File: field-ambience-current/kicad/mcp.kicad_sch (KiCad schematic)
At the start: 45 parts, among them SW1 Cell 1 (2u Choc V2 Hot-Swap), SW10 Modifier CLEAR (12x12x7.3 SMD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, SW2 Cell 2 (2u Choc V2 Hot-Swap), SW3 Cell 3 (2u Choc V2 Hot-Swap), SW4 Cell 4 (2u Choc V2 Hot-Swap), SW5 Cell 5 (2u Choc V2 Hot-Swap), SW6 Modifier SHIFT (12x12x7.3 SMD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, SW7 Modifier HOLD (12x12x7.3 SMD-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, SW8 Modifier DRONE (12x12x7.3 SMD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, SW9 Modifier GENERATE (12x12x7.3 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, U2 MCP23017-E/SS (I/O-Expander), U6 PCA9685PW (16-Ch I²C PWM LED-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

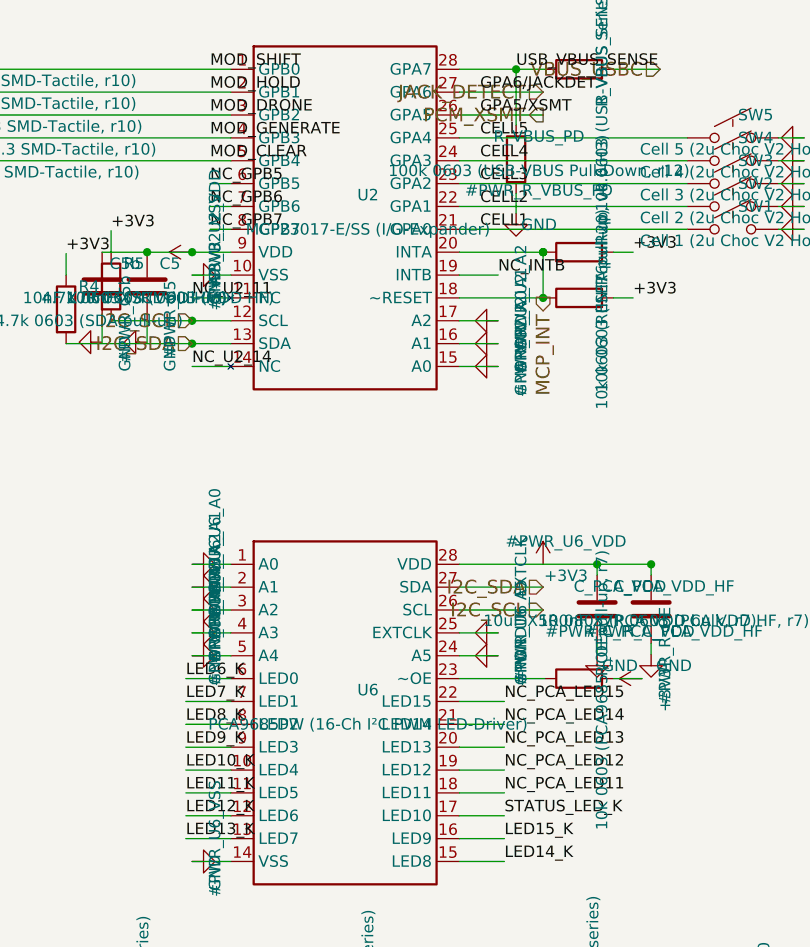
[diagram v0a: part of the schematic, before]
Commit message: pcb(r18.5): Schematic-Migration Phase 3 — STM32H743 + LCD im Generator, Repo-Audit-Fixes
KERN: generate_kicad_project.py erzeugt jetzt die H7-Architektur.

NEU stm32h743.kicad_sch (ersetzt pico.kicad_sch -> kicad/legacy_pico2/):
- 100-Pin-Symbol 1:1 aus offizieller KiCad-Lib (MCU_ST_STM32H7),
  doppelt verifiziert gegen SPEC v0.7 §5 / DS12110 Rev 5 Table 8 —
  alle 52 belegten Zuordnungen identisch (zwei unabhängige Quellen)
- alle SPEC-§5-Netze verdrahtet, 48 Reserve-GPIOs no_connect
- Support: HSE Y1 ABLS-8.000MHZ-B4-T (C596838) + 2x22pF, VCAP 2x2.2uF
  (DS12110 Tab.24), 5x(4.7uF+100nF) VDD-Bank, VDDA-Ferrit C84094 +
  1uF+100nF, BOOT0-PD 10k, NRST-PU 10k+100nF, SWD-J4 (PA13/PA14/GND),
  BAT-Teiler 100k/100k+10nF an PA3, Status-LED PD8, USB-FS PA11/PA12
  (USBLC6-ESD bleibt davor), MIDI_TX-Netz (PD5)

NEU lcd.kicad_sch (ersetzt oled.kicad_sch -> legacy): 8-Pin-ST7789
per SPEC §6 + C6b/C6c + Backlight: PCA9685-Kanal-12 -> LCD_BLK_PWM ->
2N7002 Low-Side + 100k-PD. Netze OLED_* -> LCD_*.

power_tree: U5 AP7361A-33 LDO (+5V->+3V3) + Cin 1uF/Cout 2.2uF +
EN->IN. Pico-SMPS entfällt. PICO_USB_* -> USB_DM/USB_DP.

mcp: GPB5 = VOL_SW (SPEC §5.4 — lag bis r17 entgegen der SPEC am
Pico-GPIO), PCA-Kanal 12 = LCD_BLK_PWM. Root-Brücken umgebaut,
kicad_pro-Sheetliste: Battery ergänzt (fehlte).

AUDIT-FINDINGS (verifiziert, nicht aus dem Alt-Audit übernommen):
- F-6 NEU 🔴: SPEC-§4-U5-LCSC C156144 ist ein 910R-WIDERSTAND
  (LCSC-Web verifiziert) — hätte bei JLC einen R als LDO bestückt.
  SPEC korrigiert (Kandidat C150719), Symbol trägt TBD-VERIFY.
- B-LDO 🔴: AP7361A-SOT-89-5-Pinout-Annahme (1=ADJ/NC,2=OUT,3=IN,
  4=GND,5=EN aus AP7361-DS33626-Lesart; A-Datasheet war HTTP 403) —
  als PIN_VERIFY am Symbol + PCB_LAYOUT_STATUS dokumentiert.
- B-SW12 🔴: SW6-10 (HX 12x12) auf ~6mm-TL3342-Pattern — als
  FP_MISMATCH-Property an allen 5 Symbolen markiert.
- F-2-Teilfix: Encoder-MPN -> EC11J1525402, Bourns-PEC11R-PDF nach
  datasheets/legacy/ (falsches Teil); ALPS-Drawing offen.
- F-1: T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
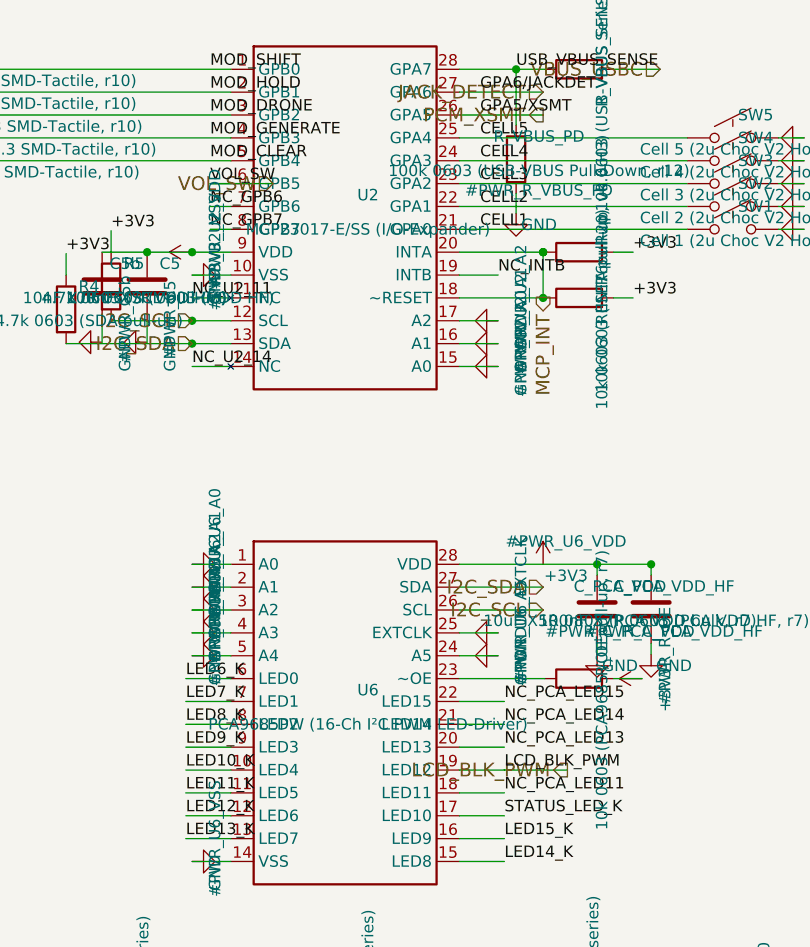
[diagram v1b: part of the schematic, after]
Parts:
- SW10, SW6, SW7, SW8, SW9: FP_MISMATCH (none) -> B-SW12: SW_SPST_TL3342 ist ein ~6mm-Land-Pattern, Teil ist 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
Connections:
- net NC_GPB5 renamed VOL_SW
- net NC_PCA_LED12 renamed LCD_BLK_PWM
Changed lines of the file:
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@@
       (property "LCSC" "C36498966" (at 87.46000000000001 98.57 0)
+        (effects (font (size 1.27 1.27)) hide))
+      (property "FP_MISMATCH" "B-SW12: SW_SPST_TL3342 ist ein ~6mm-Land-Pattern, Teil ist 12x12mm — vor Layout eigenen 12x12-SMD-FP anlegen + gegen HX-Datasheet (C36498966) pruefen" (at 87.46000000000001 99.83999999999999 0)
         (effects (font (size 1.27 1.27)) hide))
     (instances
@@
       (property "LCSC" "C36498966" (at 87.46000000000001 101.11 0)
         (effects (font (size 1.27 1.27)) hide))
+      (property "FP_MISMATCH" "B-SW12: SW_SPST_TL3342 ist ein ~6mm-Land-Pattern, Teil ist 12x12mm — vor Layout eigenen 12x12-SMD-FP anlegen + gegen HX-Datasheet (C36498966) pruefen" (at 87.46000000000001 102.38 0)
+        (effects (font (size 1.27 1.27)) hide))
     (instances
       (project "field_ambience"
@@
       (property "LCSC" "C36498966" (at 87.46000000000001 103.64999999999999 0)
         (effects (font (size 1.27 1.27)) hide))
+      (property "FP_MISMATCH" "B-SW12: SW_SPST_TL3342 ist ein ~6mm-Land-Pattern, Teil ist 12x12mm — vor Layout eigenen 12x12-SMD-FP anlegen + gegen HX-Datasheet (C36498966) pruefen" (at 87.46000000000001 104.91999999999999 0)
+        (effects (font (size 1.27 1.27)) hide))
     (instances
       (project "field_ambience"
@@
       (property "LCSC" "C36498966" (at 87.46000000000001 106.19 0)
         (effects (font (size 1.27 1.27)) hide))
+      (property "FP_MISMATCH" "B-SW12: SW_SPST_TL3342 ist ein ~6mm-Land-Pattern, Teil ist 12x12mm — vor Layout eigenen 12x12-SMD-FP anlegen + gegen HX-Datasheet (C36498966) pruefen" (at 87.46000000000001 107.46 0)
+        (effects (font (size 1.27 1.27)) hide))
     (instances
       (project "field_ambience"
@@
       (property "LCSC" "C36498966" (at 87.46000000000001 108.72999999999999 0)
         (effects (font (size 1.27 1.27)) hide))
+      (property "FP_MISMATCH" "B-SW12: SW_SPST_TL3342 ist ein ~6mm-Land-Pattern, Teil ist 12x12mm — vor Layout eigenen 12x12-SMD-FP anlegen + gegen HX-Datasheet (C36498966) pruefen" (at 87.46000000000001 109.99999999999999 0)
+        (effects (font (size 1.27 1.27)) hide))
     (instances
       (project "field_ambience"
@@
     (stroke (width 0) (type default))
 )
+  (wire (pts (xy 115 106.19) (xy 122 106.19))
+    (stroke (width 0) (type default))
+)
   (wire (pts (xy 117.3 108.72999999999999) (xy 115 108.72999999999999))
     (stroke (width 0) (type default))
@@
     (stroke (width 0) (type default))
 )
+  (wire (pts (xy 147.7 171.35000000000002) (xy 154.7 171.35000000000002))
+    (stroke (width 0) (type default))
+)
   (wire (pts (xy 142.7 168.81) (xy 147.7 168.81))
     (stroke (width 0) (type default))
@@
     (effects (font (size 1.27 1.27)) (justify left bottom))
 )
-  (label "NC_GPB5" (at 115 106.19 0) (fields_autoplaced)
+  (label "VOL_SW" (at 115 106.19 0) (fields_autoplaced)
     (effects (font (size 1.27 1.27)) (justify left bottom))
 )
@@
     (effects (font (size 1.27 1.27)) (justify left bottom))
 )
-  (label "NC_PCA_LED12" (at 147.7 171.35000000000002 0) (fields_autoplaced)
+  (label "LCD_BLK_PWM" (at 147.7 171.35000000000002 0) (fields_autoplaced)
     (effects (font (size 1.27 1.27)) (justify left bottom))
 )
@@
     (effects (font (size 1.524 1.524)) (justify right))
 )
+  (hierarchical_label "VOL_SW" (shape input) (at 122 106.19 180)
+    (effects (font (size 1.524 1.524)) (justify right))
+)
   (hierarchical_label "PCM_XSMT" (shape output) (at 152 98.57 180)
     (effects (font (size 1.524 1.524)) (justify right))
@@
     (effects (font (size 1.524 1.524)) (justify right))
 )
+  (hierarchical_label "LCD_BLK_PWM" (shape output) (at 154.7 171.35000000000002 180)
+    (effects (font (size 1.524 1.524)) (justify right))
+)

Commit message: pcb(r18.6): Engineering-Verifikation — AP7361C-Pinout-Fix, TPS61089-Quelle, Custom-FP, BOM-LCSC, ADR-MIDI
Reaktion auf User-Korrekturen aus öffentlichen Datasheets. Vier
🔴-Blocker geschlossen, einer auf eine Design-Entscheidung umklassifiziert.

=== AP7361A-Pinout war FALSCH — gefixt + AP7361C ===

r18.5-Annahme: 1=ADJ/NC, 2=OUT, 3=IN, 4=GND, 5=EN.
Korrekt (Diodes-DS via mouser.de/datasheet/3/175/1/AP7361.pdf,
User-verifiziert):
    1=EN, 2=GND, 3=ADJ/NC, 4=IN, 5=OUT

Hätte zu einem totem Board geführt (IN/OUT/EN vertauscht).

Zusätzlich:
- Symbol auf AP7361C umbenannt (Diodes markiert AP7361 als NRND ->
  use AP7361C; gleicher SOT-89-5-Pinout)
- AP7361C-33Y5-13 = LCSC C460397 (SOT-89-5) statt r18.5-Kandidat
  C150719 (= SOT-223, falsches Package; verworfen)
- Cin/Cout 4.7 µF X5R 0603 (DS-Empfehlung, statt 1µF/2.2µF)
- Symbol-Pinmap + power_tree-Verdrahtung umgebaut: EN-Pin liegt
  jetzt links oben (statt links unten), IN links unten, OUT
  rechts oben — neu gerechnete Stub-Wires + Junctions

=== TPS61089-Footprint + Datenblatt-Anchor ===

- Symbol-Pinmap (1=FSW … 11=SW) verifiziert gegen TI Rev C Tabelle 6-1
  (User-Quelle ti.com/lit/gpn/tps61089) — als PIN_SOURCE-Property
- Footprint-Name auf RNR0011A-Konvention 2.0x2.5mm VQFN-HR
- RNSR-PDF → datasheets/legacy/TPS61089RNSR_wrong_variant.pdf

=== Encoder C209762 (NRND, Prototype-OK) ===

- MPN EC11J1525402, LCSC C209762 (JLCPCB-verifiziert)
- Datasheet-Link auf JLCPCB-Detail-Seite (ALPS-Drawing nicht öffentlich)
- Status: NRND als Property — Prototype-OK, Serie braucht Ersatztyp
- FP_VERIFY-Hinweis (EC11J ist SMD, der KiCad-Standard-FP EC11E ist THT)

=== Custom-Footprint für HX 12x12 (SW6-10) ===

- libraries/field_ambience.pretty/SW_HX_12x12x7.3_SMD-4P.kicad_mod
  basierend auf LCSC-Daten von C36498966:
  - SMD-4P, 11.8x11.8mm Body, 7.3mm Höhe
  - 4 Pads je 2.5x1.5mm auf 7mm-Pitch (X+Y)
  - SPST: gegenüberliegende Pads verbunden (1↔1, 2↔2)
  - Silkscreen + Pin-1-Dot + Courtyard +0.25mm IPC-7351B
- fp-lib-table um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
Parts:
- SW10, SW6, SW7, SW8, SW9: footprint Button_Switch_SMD:SW_SPST_TL3342 -> field_ambience:SW_HX_12x12x7.3_SMD-4P; FP_MISMATCH B-SW12: SW_SPST_TL3342 ist ein ~6mm-Land-Pattern, Teil ist 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 -> (none); FP_NOTE (none) -> Custom-Footprint libraries/field_ambience.pretty/SW_HX_12x1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; Manufacturer (none) -> hanxia; Package (none) -> SMD-4P 11.8x11.8mm, vertical tactile, 7.3mm height, SPST 25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
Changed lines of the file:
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@@
       (property "Value" "Modifier SHIFT (12x12x7.3 SMD-Tactile, r10)" (at 87.46000000000001 94.75999999999999 0)
         (effects (font (size 1.27 1.27))))
-      (property "Footprint" "Button_Switch_SMD:SW_SPST_TL3342" (at 84.92 93.49 0)
+      (property "Footprint" "field_ambience:SW_HX_12x12x7.3_SMD-4P" (at 84.92 93.49 0)
         (effects (font (size 1.27 1.27)) hide))
-      (property "Datasheet" "~" (at 84.92 93.49 0)
+      (property "Datasheet" "https://www.lcsc.com/product-detail/C36498966.html" (at 84.92 93.49 0)
         (effects (font (size 1.27 1.27)) hide))
       (property "MPN" "HX 12x12x7.3TPFT-B" (at 87.46000000000001 97.3 0)
         (effects (font (size 1.27 1.27)) hide))
-      (property "LCSC" "C36498966" (at 87.46000000000001 98.57 0)
+      (property "Manufacturer" "hanxia" (at 87.46000000000001 98.57 0)
         (effects (font (size 1.27 1.27)) hide))
-      (property "FP_MISMATCH" "B-SW12: SW_SPST_TL3342 ist ein ~6mm-Land-Pattern, Teil ist 12x12mm — vor Layout eigenen 12x12-SMD-FP anlegen + gegen HX-Datasheet (C36498966) pruefen" (at 87.46000000000001 99.83999999999999 0)
+      (property "LCSC" "C36498966" (at 87.46000000000001 99.83999999999999 0)
+        (effects (font (size 1.27 1.27)) hide))
+      (property "Package" "SMD-4P 11.8x11.8mm, vertical tactile, 7.3mm height, SPST 250gf, 100k cycles, 12V/50mA" (at 87.46000000000001 101.11 0)
+        (effects (font (size 1.27 1.27)) hide))
+      (property "FP_NOTE" "Custom-Footprint libraries/field_ambience.pretty/SW_HX_12x12x7.3_SMD-4P.kicad_mod (User-Daten + LCSC C36498966). 4 Pads je 2.5x1.5mm auf 7mm-Pitch (X+Y); SPST: gegenüberliegende Pads sind elektrisch verbunden (1↔1, 2↔2)." (at 87.46000000000001 102.38 0)
         (effects (font (size 1.27 1.27)) hide))
     (instances
@@
       (property "Value" "Modifier HOLD (12x12x7.3 SMD-Tactile, r10)" (at 87.46000000000001 97.3 0)
         (effects (font (size 1.27 1.27))))
-      (property "Footprint" "Button_Switch_SMD:SW_SPST_TL3342" (at 84.92 96.03 0)
+      (property "Footprint" "field_ambience:SW_HX_12x12x7.3_SMD-4P" (at 84.92 96.03 0)
         (effects (font (size 1.27 1.27)) hide))
-      (property "Datasheet" "~" (at 84.92 96.03 0)
+      (property "Datasheet" "https://www.lcsc.com/product-detail/C36498966.html" (at 84.92 96.03 0)
         (effects (font (size 1.27 1.27)) hide))
       (property "MPN" "HX 12x12x7.3TPFT-B" (at 87.46000000000001 99.84 0)
         (effects (font (size 1.27 1.27)) hide))
-      (property "LCSC" "C36498966" (at 87.46000000000001 101.11 0)
+      (property "Manufacturer" "hanxia" (at 87.46000000000001 101.11 0)
         (effects (font (size 1.27 1.27)) hide))
-      (property "FP_MISMATCH" "B-SW12: SW_SPST_TL3342 ist ein ~6mm-Land-Pattern, Teil ist 12x12mm — vor Layout eigenen 12x12-SMD-FP anlegen + gegen HX-Datasheet (C36498966) pruefen" (at 87.46000000000001 102.38 0)
+      (property "LCSC" "C36498966" (at 87.46000000000001 102.38 0)
+        (effects (font (size 1.27 1.27)) hide))
+      (property "Package" "SMD-4P 11.8x11.8mm, vertical tactile, 7.3mm height, SPST 250gf, 100k cycles, 12V/50mA" (at 87.46000000000001 103.65 0)
+        (effects (font (size 1.27 1.27)) hide))
+      (property "FP_NOTE" "Custom-Footprint libraries/field_ambience.pretty/SW_HX_12x12x7.3_SMD-4P.kicad_mod (User-Daten + LCSC C36498966). 4 Pads je 2.5x1.5mm auf 7mm-Pitch (X+Y); SPST: gegenüberliegende Pads sind elektrisch verbunden (1↔1, 2↔2)." (at 87.46000000000001 104.92 0)
         (effects (font (size 1.27 1.27)) hide))
     (instances
@@
       (property "Value" "Modifier DRONE (12x12x7.3 SMD-Tactile, r10)" (at 87.46000000000001 99.83999999999999 0)
         (effects (font (size 1.27 1.27))))
-      (property "Footprint" "Button_Switch_SMD:SW_SPST_TL3342" (at 84.92 98.57 0)
+      (property "Footprint" "field_ambience:SW_HX_12x12x7.3_SMD-4P" (at 84.92 98.57 0)
         (effects (font (size 1.27 1.27)) hide))
-      (property "Datasheet" "~" (at 84.92 98.57 0)
+      (property "Datasheet" "https://www.lcsc.com/product-detail/C36498966.html" (at 84.92 98.57 0)
         (effects (font (size 1.27 1.27)) hide))
       (property "MPN" "HX 12x12x7.3TPFT-B" (at 87.46000000000001 102.38 0)
         (effects (font (size 1.27 1.27)) hide))
-      (property "LCSC" "C36498966" (at 87.46000000000001 103.64999999999999 0)
+      (property "Manufacturer" "hanxia" (at 87.46000000000001 103.64999999999999 0)
         (effects (font (size 1.27 1.27)) hide))
-      (property "FP_MISMATCH" "B-SW12: SW_SPST_TL3342 ist ein ~6mm-Land-Pattern, Teil ist 12x12mm — vor Layout eigenen 12x12-SMD-FP anlegen + gegen HX-Datasheet (C36498966) pruefen" (at 87.46000000000001 104.91999999999999 0)
+      (property "LCSC" "C36498966" (at 87.46000000000001 104.91999999999999 0)
+        (effects (font (size 1.27 1.27)) hide))
+      (property "Package" "SMD-4P 11.8x11.8mm, vertical tactile, 7.3mm height, SPST 250gf, 100k cycles, 12V/50mA" (at 87.46000000000001 106.19 0)
+        (effects (font (size 1.27 1.27)) hide))
+      (property "FP_NOTE" "Custom-Footprint libraries/field_ambience.pretty/SW_HX_12x12x7.3_SMD-4P.kicad_mod (User-Daten + LCSC C36498966). 4 Pads je 2.5x1.5mm auf 7mm-Pitch (X+Y); SPST: gegenüberliegende Pads sind elektrisch verbunden (1↔1, 2↔2)." (at 87.46000000000001 107.46 0)
         (effects (font (size 1.27 1.27)) hide))
     (instances
@@
       (property "Value" "Modifier GENERATE (12x12x7.3 SMD-Tactile, r10)" (at 87.46000000000001 102.38 0)
         (effects (font (size 1.27 1.27))))
-      (property "Footprint" "Button_Switch_SMD:SW_SPST_TL3342" (at 84.92 101.11 0)
+      (property "Footprint" "field_ambience:SW_HX_12x12x7.3_SMD-4P" (at 84.92 101.11 0)
         (effects (font (size 1.27 1.27)) hide))
-      (property "Datasheet" "~" (at 84.92 101.11 0)
+      (property "Datasheet" "https://www.lcsc.com/product-detail/C36498966.html" (at 84.92 101.11 0)
         (effects (font (size 1.27 1.27)) hide))
       (property "MPN" "HX 12x12x7.3TPFT-B" (at 87.46000000000001 104.92 0)
         (effects (font (size 1.27 1.27)) hide))
-      (property "LCSC" "C36498966" (at 87.46000000000001 106.19 0)
+      (property "Manufacturer" "hanxia" (at 87.46000000000001 106.19 0)
         (effects (font (size 1.27 1.27)) hide))
-      (property "FP_MISMATCH" "B-SW12: SW_SPST_TL3342 ist ein ~6mm-Land-Pattern, Teil ist 12x12mm — vor Layout eigenen 12x12-SMD-FP anlegen + gegen HX-Datasheet (C36498966) pruefen" (at 87.46000000000001 107.46 0)
+      (property "LCSC" "C36498966" (at 87.46000000000001 107.46 0)
+        (effects (font (size 1.27 1.27)) hide))
+      (property "Package" "SMD-4P 11.8x11.8mm, vertical tactile, 7.3mm height, SPST 250gf, 100k cycles, 12V/50mA" (at 87.46000000000001 108.73 0)
+        (effects (font (size 1.27 1.27)) hide))
+      (property "FP_NOTE" "Custom-Footprint libraries/field_ambience.pretty/SW_HX_12x12x7.3_SMD-4P.kicad_mod (User-Daten + LCSC C36498966). 4 Pads je 2.5x1.5mm auf 7mm-Pitch (X+Y); SPST: gegenüberliegende Pads sind elektrisch verbunden (1↔1, 2↔2)." (at 87.46000000000001 110.0 0)
         (effects (font (size 1.27 1.27)) hide))
     (instances
@@
       (property "Value" "Modifier CLEAR (12x12x7.3 SMD-Tactile, r10)" (at 87.46000000000001 104.91999999999999 0)
         (effects (font (size 1.27 1.27))))
-      (property "Footprint" "Button_Switch_SMD:SW_SPST_TL3342" (at 84.92 103.64999999999999 0)
+      (property "Footprint" "field_ambience:SW_HX_12x12x7.3_SMD-4P" (at 84.92 103.64999999999999 0)
         (effects (font (size 1.27 1.27)) hide))
-      (property "Datasheet" "~" (at 84.92 103.64999999999999 0)
+      (property "Datasheet" "https://www.lcsc.com/product-detail/C36498966.html" (at 84.92 103.64999999999999 0)
         (effects (font (size 1.27 1.27)) hide))
       (property "MPN" "HX 12x12x7.3TPFT-B" (at 87.46000000000001 107.46 0)
         (effects (font (size 1.27 1.27)) hide))
-      (property "LCSC" "C36498966" (at 87.46000000000001 108.72999999999999 0)
+      (property "Manufacturer" "hanxia" (at 87.46000000000001 108.72999999999999 0)
         (effects (font (size 1.27 1.27)) hide))
-      (property "FP_MISMATCH" "B-SW12: SW_SPST_TL3342 ist ein ~6mm-Land-Pattern, Teil ist 12x12mm — vor Layout eigenen 12x12-SMD-FP anlegen + gegen HX-Datasheet (C36498966) pruefen" (at 87.46000000000001 109.99999999999999 0)
+      (property "LCSC" "C36498966" (at 87.46000000000001 109.99999999999999 0)
+        (effects (font (size 1.27 1.27)) hide))
+      (property "Package" "SMD-4P 11.8x11.8mm, vertical tactile, 7.3mm height, SPST 250gf, 100k cycles, 12V/50mA" (at 87.46000000000001 111.27 0)
+        (effects (font (size 1.27 1.27)) hide))
+      (property "FP_NOTE" "Custom-Footprint libraries/field_ambience.pretty/SW_HX_12x12x7.3_SMD-4P.kicad_mod (User-Daten + LCSC C36498966). 4 Pads je 2.5x1.5mm auf 7mm-Pitch (X+Y); SPST: gegenüberliegende Pads sind elektrisch verbunden (1↔1, 2↔2)." (at 87.46000000000001 112.53999999999999 0)
         (effects (font (size 1.27 1.27)) hide))
     (instances
